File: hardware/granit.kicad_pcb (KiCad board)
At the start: 4 copper layers, 92 x 100 mm, 107 parts, among them IC1 ASM1061, J1 12V Barrel, J2 12V Screw Terminal, J3 RJ45_RB1-125B8G1A, J6 Conn_01x02, J7 USB_C_Receptacle_USB2.0_14P, J8 Conn_01x03, J9 SATA_22pin, Q1 FDS4435BZ, Q2 FDS4435BZ, Q3 FDS4435BZ, Q4 2N7002, Q5 2N7002, Q6 2N7002, SW1 SW_Push, U1 NCP1117-3.3_SOT223, U2 AP64501SP-13, U3 74AHCT1G125, U4 DS3231MZ, U5 USBLC6-2SC6, U6 74AHCT1G32, Y1 Crystal

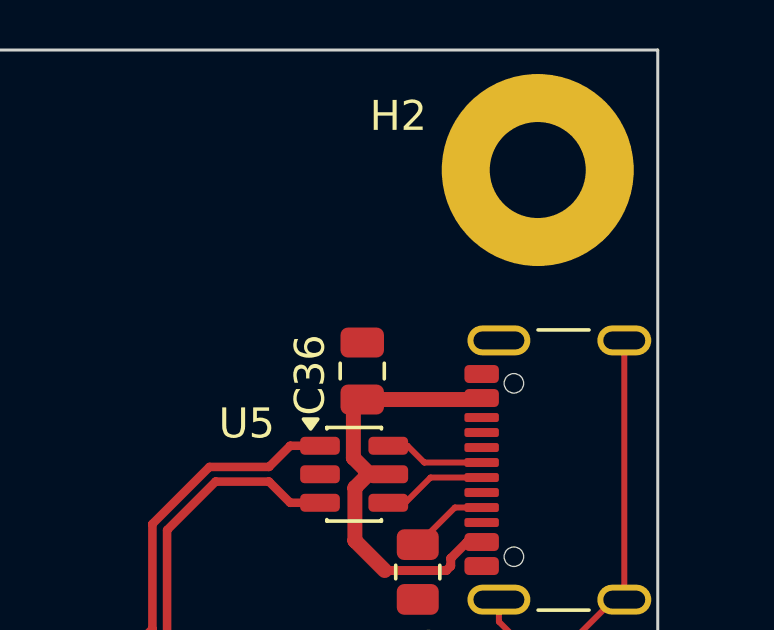
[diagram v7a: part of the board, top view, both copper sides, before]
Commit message: Fix fiducial footprint name to Fiducial_1mm_Mask2mm
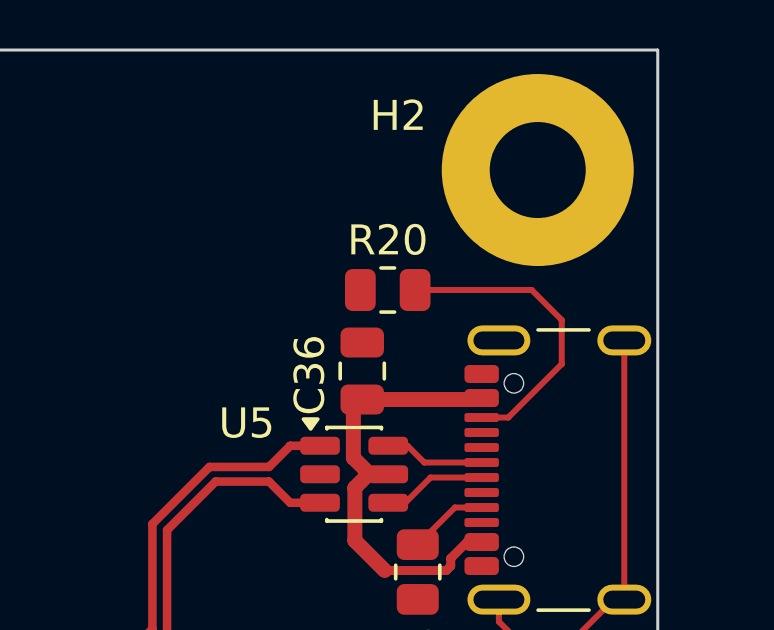
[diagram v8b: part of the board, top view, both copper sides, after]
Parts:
- added R20: 5K1, Resistor_SMD:R_0805_2012Metric, F.Cu at (103.0, 28.0)
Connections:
- CM1 pad 30: GPIO_HOLD -> SATA_PWR_EN
- CM1 pad 34: SATA_PWR_EN -> GPIO_HOLD
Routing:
- net Net-(J7-CC2): track 0.00 -> 10.2 mm
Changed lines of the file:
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@@
 		)
 	)
+	(footprint "Resistor_SMD:R_0805_2012Metric"
+		(layer "F.Cu")
+		(at 103 28)
+		(descr "Resistor SMD 0805 (2012 Metric), square (rectangular) end terminal, IPC-7351 nominal, (Body size source: IPC-SM-782 page 72, https://www.pcb-3d.com/wordpress/wp-content/uploads/ipc-sm-782a_amendment_1_and_2.pdf)")
+		(tags "resistor")
+		(property "Reference" "R20"
+			(at 0 -1.65 0)
+			(layer "F.SilkS")
+			(effects
+				(font
+					(size 1 1)
+					(thickness 0.15)
+				)
+			)
+		)
+		(property "Value" "5K1"
+			(at 0 1.65 0)
+			(layer "F.Fab")
+			(effects
+				(font
+					(size 1 1)
+					(thickness 0.15)
+				)
+			)
+		)
+		(property "Datasheet" ""
+			(at 0 0 0)
+			(layer "F.Fab")
+			(hide yes)
+			(effects
+				(font
+					(size 1.27 1.27)
+				)
+			)
+		)
+		(property "Description" "Resistor, small symbol"
+			(at 0 0 0)
+			(layer "F.Fab")
+			(hide yes)
+			(effects
+				(font
+					(size 1.27 1.27)
+				)
+			)
+		)
+		(property "KiLib_Generator" "SMD_2terminal_chip_molded"
+			(at 0 0 0)
+			(layer "F.SilkS")
+			(hide yes)
+			(effects
+				(font
+					(size 1 1)
+					(thickness 0.15)
+				)
+			)
+		)
+		(property ki_fp_filters "R_*")
+		(sheetname "/Peripherals/")
+		(sheetfile "peripherals.kicad_sch")
+		(units
+			(unit
+				(name "A")
+				(pins "1" "2")
+			)
+		)
+		(attr smd)
+		(duplicate_pad_numbers_are_jumpers no)
+		(fp_line
+			(start -0.227064 -0.735)
+			(end 0.227064 -0.735)
+			(stroke
+				(width 0.12)
+				(type solid)
+			)
+			(layer "F.SilkS")
+		)
+		(fp_line
+			(start -0.227064 0.735)
+			(end 0.227064 0.735)
+			(stroke
+				(width 0.12)
+				(type solid)
+			)
+			(layer "F.SilkS")
+		)
+		(fp_poly
+			(pts
+				(xy -1.68 -0.95) (xy 1.68 -0.95) (xy 1.68 0.95) (xy -1.68 0.95)
+			)
+			(stroke
+				(width 0.05)
+				(type solid)
+			)
+			(fill no)
+			(layer "F.CrtYd")
+		)
+		(fp_poly
+			(pts
+				(xy -1 -0.625) (xy 1 -0.625) (xy 1 0.625) (xy -1 0.625)
+			)
+			(stroke
+				(width 0.1)
+				(type solid)
+			)
+			(fill no)
+			(layer "F.Fab")
+		)
+		(fp_text user "${REFERENCE}"
+			(at 0 0 0)
+			(layer "F.Fab")
+			(effects
+				(font
+					(size 0.5 0.5)
+					(thickness 0.08)
+				)
+			)
+		)
+		(pad "1" smd roundrect
+			(at -0.9125 0)
+			(size 1.025 1.4)
+			(layers "F.Cu" "F.Mask" "F.Paste")
+			(roundrect_rratio 0.243902)
+			(net "GND")
+			(pintype "passive")
+		)
+		(pad "2" smd roundrect
+			(at 0.9125 0)
+			(size 1.025 1.4)
+			(layers "F.Cu" "F.Mask" "F.Paste")
+			(roundrect_rratio 0.243902)
+			(net "Net-(J7-CC2)")
+			(pintype "passive")
+		)
+		(embedded_fonts no)
+		(model "${KICAD10_3DMODEL_DIR}/Resistor_SMD.3dshapes/R_0805_2012Metric.step"
+			(offset
+				(xyz 0 0 0)
+			)
+			(scale
+				(xyz 1 1 1)
+			)
+			(rotate
+				(xyz 0 0 0)
+			)
+		)
+	)
 	(footprint "LED_SMD:LED_0805_2012Metric"
 		(layer "F.Cu")
@@
 			(size 0.2 0.7)
 			(layers "F.Cu" "F.Mask" "F.Paste")
-			(net "GPIO_HOLD")
+			(net "SATA_PWR_EN")
 			(pinfunction "GPIO6_30")
 			(pintype "passive")
@@
 			(size 0.2 0.7)
 			(layers "F.Cu" "F.Mask" "F.Paste")
-			(net "SATA_PWR_EN")
+			(net "GPIO_HOLD")
 			(pinfunction "GPIO5_34")
 			(pintype "passive")
@@
 	)
 	(segment
+		(start 107.019594 32.25)
+		(end 108.8 30.469594)
+		(width 0.2)
+		(layer "F.Cu")
+		(net "Net-(J7-CC2)")
+	)
+	(segment
+		(start 108.8 29)
+		(end 107.8 28)
+		(width 0.2)
+		(layer "F.Cu")
+		(net "Net-(J7-CC2)")
+	)
+	(segment
+		(start 108.8 30.469594)
+		(end 108.8 29)
+		(width 0.2)
+		(layer "F.Cu")
+		(net "Net-(J7-CC2)")
+	)
+	(segment
+		(start 107.8 28)
+		(end 103.9125 28)
+		(width 0.2)
+		(layer "F.Cu")
+		(net "Net-(J7-CC2)")
+	)
+	(segment
+		(start 106.13 32.25)
+		(end 107.019594 32.25)
+		(width 0.2)
+		(layer "F.Cu")
+		(net "Net-(J7-CC2)")
+	)
+	(segment
